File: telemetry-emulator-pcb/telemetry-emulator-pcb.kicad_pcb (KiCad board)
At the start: 2 copper layers, 100 x 50 mm, 53 parts, among them IC1 ATmega328P-A, IC2 MCP2515-xSO, IC3 MCP2551-I-SN, J1 USB_B_Micro, J2 ENABLE_RX, J3 Conn_02x13_Odd_Even, J4 CAN_TERM, J5 USE_V_INT, J6 UART, J7 CAN, J8 CAN, J9 CAN, Q1 BSS138, Q2 BSS138, U1 CH340C, Y1 16MHz, Y2 8MHz

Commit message: done and done
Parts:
- added R7: 10K, Resistor_SMD:R_0805_2012Metric, F.Cu at (100.5, 78.5)
- renumbered R9 to R10, R10 to R11, R11 to R12, R12 to R13, R7 to R8, R8 to R9
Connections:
- IC2 pad 17: +5V -> Net-(IC2-Pad17)
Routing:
- net Net-(IC2-Pad17): track 0.00 -> 14.0 mm, vias 0 -> 2
- net MOSI: track 70.1 -> 72.8 mm
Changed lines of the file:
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@@
   (net 66 "Net-(J4-Pad1)")
   (net 67 "V_EXT")
+  (net 68 "Net-(IC2-Pad17)")
   (footprint "Capacitor_SMD:C_0805_2012Metric" (layer "F.Cu")
     (at 157.48 92.642)
@@
     (property "Sheetname" "")
     (attr smd)
-    (fp_text reference "R11" (at 2.653 0.0325 180) (layer "F.SilkS")
+    (fp_text reference "R12" (at 2.653 0.0325 180) (layer "F.SilkS")
       (effects (font (size 1 1) (thickness 0.15)))
     )
@@
       (net 21 "CAN_CS") (pinfunction "~{CS}") (pintype "input"))
     (pad "17" smd roundrect (at 4.65 -3.81 270) (size 2.05 0.6) (layers "F.Cu" "F.Paste" "F.Mask") (roundrect_rratio 0.25)
-      (net 1 "+5V") (pinfunction "~{RESET}") (pintype "input"))
+      (net 68 "Net-(IC2-Pad17)") (pinfunction "~{RESET}") (pintype "input"))
     (pad "18" smd roundrect (at 4.65 -5.08 270) (size 2.05 0.6) (layers "F.Cu" "F.Paste" "F.Mask") (roundrect_rratio 0.25)
       (net 1 "+5V") (pinfunction "VDD") (pintype "power_in"))
@@
     (property "Sheetname" "")
     (attr smd)
-    (fp_text reference "R9" (at 0 -1.65 90) (layer "F.SilkS")
+    (fp_text reference "R10" (at 0 -1.65 90) (layer "F.SilkS")
       (effects (font (size 1 1) (thickness 0.15)))
     )
@@
     (property "Sheetname" "")
     (attr smd)
-    (fp_text reference "R12" (at 0 -1.65) (layer "F.SilkS")
+    (fp_text reference "R13" (at 0 -1.65) (layer "F.SilkS")
       (effects (font (size 1 1) (thickness 0.15)))
     )
@@
   )
   (footprint "Resistor_SMD:R_0805_2012Metric" (layer "F.Cu")
+    (at 100.5 78.5 90)
+    (descr "Resistor SMD 0805 (2012 Metric), square (rectangular) end terminal, IPC_7351 nominal, (Body size source: IPC-SM-782 page 72, https://www.pcb-3d.com/wordpress/wp-content/uploads/ipc-sm-782a_amendment_1_and_2.pdf), generated with kicad-footprint-generator")
+    (tags "resistor")
+    (property "Sheetfile" "telemetry-emulator-pcb.kicad_sch")
+    (property "Sheetname" "")
+    (attr smd)
+    (fp_text reference "R7" (at 2.4 0 180) (layer "F.SilkS")
+      (effects (font (size 1 1) (thickness 0.15)))
+    )
+    (fp_text value "10K" (at 0.2 -1.7 270) (layer "F.Fab")
+      (effects (font (size 1 1) (thickness 0.15)))
+    )
+    (fp_text user "${REFERENCE}" (at 0 0 90) (layer "F.Fab")
+      (effects (font (size 0.5 0.5) (thickness 0.08)))
+    )
+    (fp_line (start -0.227064 0.735) (end 0.227064 0.735) (layer "F.SilkS") (width 0.12))
+    (fp_line (start -0.227064 -0.735) (end 0.227064 -0.735) (layer "F.SilkS") (width 0.12))
+    (fp_line (start 1.68 -0.95) (end 1.68 0.95) (layer "F.CrtYd") (width 0.05))
+    (fp_line (start -1.68 0.95) (end -1.68 -0.95) (layer "F.CrtYd") (width 0.05))
+    (fp_line (start -1.68 -0.95) (end 1.68 -0.95) (layer "F.CrtYd") (width 0.05))
+    (fp_line (start 1.68 0.95) (end -1.68 0.95) (layer "F.CrtYd") (width 0.05))
+    (fp_line (start 1 0.625) (end -1 0.625) (layer "F.Fab") (width 0.1))
+    (fp_line (start -1 -0.625) (end 1 -0.625) (layer "F.Fab") (width 0.1))
+    (fp_line (start 1 -0.625) (end 1 0.625) (layer "F.Fab") (width 0.1))
+    (fp_line (start -1 0.625) (end -1 -0.625) (layer "F.Fab") (width 0.1))
+    (pad "1" smd roundrect (at -0.9125 0 90) (size 1.025 1.4) (layers "F.Cu" "F.Paste" "F.Mask") (roundrect_rratio 0.243902)
+      (net 68 "Net-(IC2-Pad17)") (pintype "passive"))
+    (pad "2" smd roundrect (at 0.9125 0 90) (size 1.025 1.4) (layers "F.Cu" "F.Paste" "F.Mask") (roundrect_rratio 0.243902)
+      (net 1 "+5V") (pintype "passive"))
+    (model "${KICAD6_3DMODEL_DIR}/Resistor_SMD.3dshapes/R_0805_2012Metric.wrl"
+      (offset (xyz 0 0 0))
+      (scale (xyz 1 1 1))
+      (rotate (xyz 0 0 0))
+    )
+  )
+  (footprint "Resistor_SMD:R_0805_2012Metric" (layer "F.Cu")
     (at 158.7325 79.8595 -90)
     (descr "Resistor SMD 0805 (2012 Metric), square (rectangular) end terminal, IPC_7351 nominal, (Body size source: IPC-SM-782 page 72, https://www.pcb-3d.com/wordpress/wp-content/uploads/ipc-sm-782a_amendment_1_and_2.pdf), generated with kicad-footprint-generator")
@@
     (property "Sheetname" "")
     (attr smd)
-    (fp_text reference "R7" (at -2.4595 0.0325 180) (layer "F.SilkS")
+    (fp_text reference "R8" (at -2.4595 0.0325 180) (layer "F.SilkS")
       (effects (font (size 1 1) (thickness 0.15)))
     )
@@
     (property "Sheetname" "")
     (attr smd)
-    (fp_text reference "R10" (at -2.4595 0.0325 180) (layer "F.SilkS")
+    (fp_text reference "R11" (at -2.4595 0.0325 180) (layer "F.SilkS")
       (effects (font (size 1 1) (thickness 0.15)))
     )
@@
     (property "Sheetname" "")
     (attr smd)
-    (fp_text reference "R8" (at 2.6405 0.0325 180) (layer "F.SilkS")
+    (fp_text reference "R9" (at 2.6405 0.0325 180) (layer "F.SilkS")
       (effects (font (size 1 1) (thickness 0.15)))
     )
@@
   (segment (start 136.684 89.73) (end 136.684 84.106) (width 0.25) (layer "F.Cu") (net 9))
   (segment (start 136 91.3) (end 136 91.274198) (width 0.25) (layer "F.Cu") (net 9))
+  (segment (start 108.6 77.9) (end 108.712 78.012) (width 0.25) (layer "F.Cu") (net 9))
   (segment (start 136.687099 89.733099) (end 136.684 89.73) (width 0.25) (layer "F.Cu") (net 9))
   (segment (start 136 91.274198) (end 136.687099 90.587099) (width 0.25) (layer "F.Cu") (net 9))
+  (segment (start 108.712 78.012) (end 108.712 83.136) (width 0.25) (layer "F.Cu") (net 9))
   (segment (start 136.687099 90.587099) (end 136.687099 89.733099) (width 0.25) (layer "F.Cu") (net 9))
-  (segment (start 108.712 79.912) (end 108.712 83.136) (width 0.25) (layer "F.Cu") (net 9))
   (segment (start 136.684 84.106) (end 133.35 80.772) (width 0.25) (layer "F.Cu") (net 9))
-  (segment (start 108.7 79.9) (end 108.712 79.912) (width 0.25) (layer "F.Cu") (net 9))
-  (via (at 108.7 79.9) (size 0.8) (drill 0.4) (layers "F.Cu" "B.Cu") (free) (net 9))
+  (via (at 108.6 77.9) (size 0.8) (drill 0.4) (layers "F.Cu" "B.Cu") (free) (net 9))
   (via (at 136 91.3) (size 0.8) (drill 0.4) (layers "F.Cu" "B.Cu") (free) (net 9))
-  (segment (start 130.1 79.5) (end 132.078 79.5) (width 0.25) (layer "B.Cu") (net 9))
+  (segment (start 131.985 79.407) (end 133.35 80.772) (width 0.25) (layer "B.Cu") (net 9))
   (segment (start 115.54 103.46) (end 114.94 103.46) (width 0.25) (layer "B.Cu") (net 9))
-  (segment (start 132.078 79.5) (end 133.35 80.772) (width 0.25) (layer "B.Cu") (net 9))
+  (segment (start 128.828 78.6) (end 129.635 79.407) (width 0.25) (layer "B.Cu") (net 9))
   (segment (start 135.5 90.8) (end 135.5 89.5) (width 0.25) (layer "B.Cu") (net 9))
-  (segment (start 108.7 79.9) (end 129.7 79.9) (width 0.25) (layer "B.Cu") (net 9))
-  (segment (start 129.7 79.9) (end 130.1 79.5) (width 0.25) (layer "B.Cu") (net 9))
   (segment (start 135.5 89.5) (end 135 89) (width 0.25) (layer "B.Cu") (net 9))
+  (segment (start 129.635 79.407) (end 131.985 79.407) (width 0.25) (layer "B.Cu") (net 9))
   (segment (start 135 89) (end 130.036396 89) (width 0.25) (layer "B.Cu") (net 9))
+  (segment (start 108.6 77.9) (end 109.3 78.6) (width 0.25) (layer "B.Cu") (net 9))
   (segment (start 130.036396 89) (end 115.576396 103.46) (width 0.25) (layer "B.Cu") (net 9))
   (segment (start 115.576396 103.46) (end 114.94 103.46) (width 0.25) (layer "B.Cu") (net 9))
   (segment (start 136 91.3) (end 135.5 90.8) (width 0.25) (layer "B.Cu") (net 9))
+  (segment (start 109.3 78.6) (end 128.828 78.6) (width 0.25) (layer "B.Cu") (net 9))
   (segment (start 137.4 95.621) (end 139.084 97.305) (width 0.25) (layer "F.Cu") (net 10))
   (segment (start 137.4 95.1045) (end 137.4 95.621) (width 0.25) (layer "F.Cu") (net 10))
@@
   (segment (start 173.078897 80.039897) (end 171.2885 78.2495) (width 0.25) (layer "B.Cu") (net 67))
   (segment (start 171.9305 87.4) (end 173.078897 86.251603) (width 0.25) (layer "B.Cu") (net 67))
+  (via (at 112.5 83.2) (size 0.8) (drill 0.4) (layers "F.Cu" "B.Cu") (net 68))
+  (via (at 100.5 79.4) (size 0.8) (drill 0.4) (layers "F.Cu" "B.Cu") (net 68))
+  (segment (start 102.3 81.2) (end 111.3 81.2) (width 0.25) (layer "B.Cu") (net 68))
+  (segment (start 100.5 79.4) (end 102.3 81.2) (width 0.25) (layer "B.Cu") (net 68))
+  (segment (start 111.3 81.2) (end 112.5 82.4) (width 0.25) (layer "B.Cu") (net 68))
+  (segment (start 112.5 82.4) (end 112.5 83.2) (width 0.25) (layer "B.Cu") (net 68))
   (zone (net 1) (net_name "+5V") (layer "F.Cu") (name "5V") (hatch edge 0.508)
     (connect_pads (clearance 0.508))

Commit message: Board is finished
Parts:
- removed the C3 at (108.2, 88.7)
- removed the C3 at (94.3, 73.7)
- added C3: 10uF, Capacitor_SMD:C_1206_3216Metric, F.Cu at (94.4, 73.2)
- added C7: 0.1uF, Capacitor_SMD:C_0805_2012Metric, F.Cu at (108.2, 88.7)
- added D5: Schottky, Diode_SMD:D_SOD-323, F.Cu at (170.4, 71.4)
- C1: footprint Capacitor_SMD:C_0805_2012Metric -> Diode_SMD:D_SOD-323
- D2: value purple -> red
- IC1: value ATmega328P-A -> ATmega328P
- IC2: value MCP2515-xSO -> MCP2515
- IC3: value MCP2551-I-SN -> MCP2551
- J1: value USB_B_Micro -> USB
- J2: value ENABLE_RX -> RX_TX; footprint Connector_PinHeader_2.54mm:PinHeader_1x02_P2.54mm_Vertical -> Connector_PinHeader_2.54mm:PinHeader_2x02_P2.54mm_Vertical
- J3: value Conn_02x13_Odd_Even -> GPIO
- J5: value USE_V_INT -> V_INT
- R1: value 1K -> 1.2K
- R2: value 500 -> 1.5K
- R3: value 1K -> 1.5K
- R4: value 500 -> 1.2K
- moved J5 3.50 mm to (174.9, 93.9)
- moved J2 3.30 mm to (168.4, 96.6), turned to 90 degrees
- turned C2 to -90 degrees
- renumbered C8 to C10, C9 to C11, C10 to C12, C11 to C13, C2 to C4, C4 to C5, C5 to C6, C6 to C8, C7 to C9
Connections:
- C2 pad 1: +5V -> Earth
- C2 pad 2: Earth -> +5V
- IC1 pad 31: TX -> TX_USB
- J2 pad 1: RX -> RX_USB
- J2 pad 2: RX_USB -> RX
- J3 pad 26: TX -> TX_USB
- J6 pad 1: V_EXT -> Net-(D5-Pad2)
- J7 pad 1: CANH -> CANL
- J7 pad 2: CANL -> CANH
- J8 pad 1: CANH -> CANL
- J8 pad 2: CANL -> CANH
- J9 pad 1: CANH -> CANL
- J9 pad 2: CANL -> CANH
- R13 pad 2: CANL -> CANH
- R6 pad 1: TX -> TX_USB
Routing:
- net TX_USB: track 0.00 -> 60.4 mm, vias 0 -> 2
- net TX: track 78.4 -> 22.1 mm, vias 5 -> 1
- net CANL: track 58.2 -> 40.5 mm
- net Net-(D5-Pad2): track 0.00 -> 8.37 mm
- net CANH: track 51.2 -> 57.2 mm
- net V_EXT: track 44.1 -> 47.8 mm, vias 2 -> 3
- net RX_USB: track 58.3 -> 61.2 mm, vias 2 -> 3
- net D7: track 55.5 -> 53.8 mm
- net D6: track 51.4 -> 49.9 mm
- net +5V: track 24.0 -> 24.8 mm
- net D5: track 43.2 -> 42.4 mm
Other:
- board text added: "Colby Sparks Silviu Toderita"
- board text added: "Telemetry Emulator 1.0"
- board text added: "UBC Supermileage"

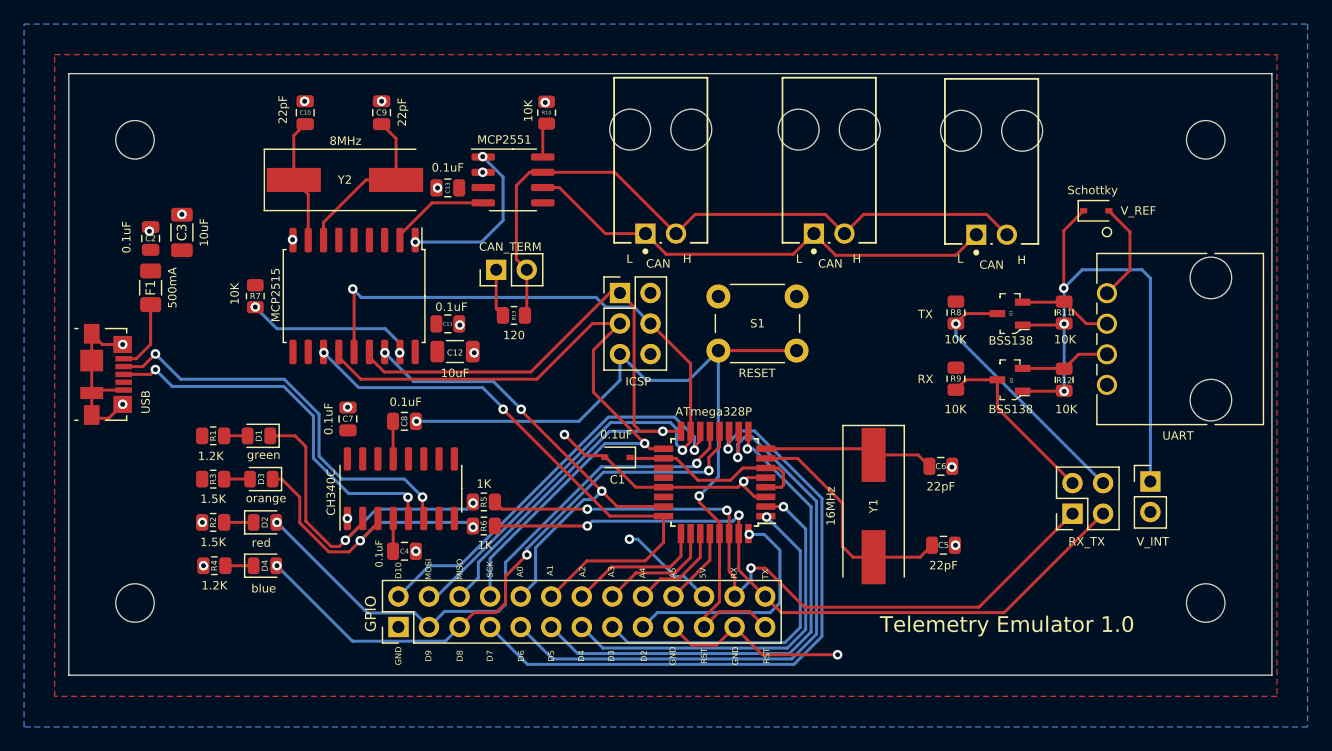
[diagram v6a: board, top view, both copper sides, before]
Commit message: adds rounded edges to pcb and modifies xtal resistance
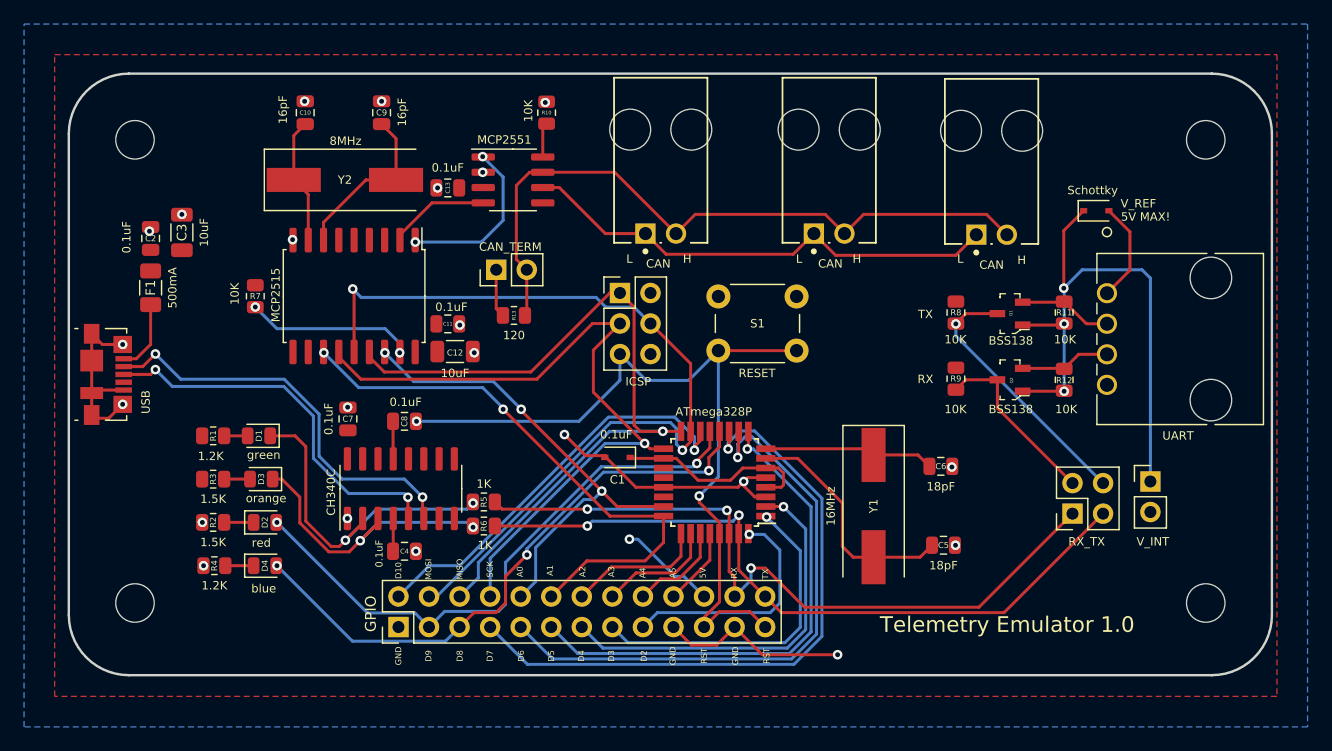
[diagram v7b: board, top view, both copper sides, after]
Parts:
- C10, C9: value 22pF -> 16pF
- C5, C6: value 22pF -> 18pF
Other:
- outline, holes or cut-outs redrawn
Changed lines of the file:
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@@
       (effects (font (size 0.7 0.7) (thickness 0.1)))
     )
-    (fp_text value "22pF" (at 0 1.68) (layer "F.SilkS")
+    (fp_text value "18pF" (at 0 1.68) (layer "F.SilkS")
       (effects (font (size 0.7 0.7) (thickness 0.1)))
     )
@@
       (effects (font (size 0.7 0.7) (thickness 0.1)))
     )
-    (fp_text value "22pF" (at 0 1.68) (layer "F.SilkS")
+    (fp_text value "18pF" (at 0 1.68) (layer "F.SilkS")
       (effects (font (size 0.7 0.7) (thickness 0.1)))
     )
@@
       (effects (font (size 0.7 0.7) (thickness 0.1)))
     )
-    (fp_text value "22pF" (at 0.246 -1.848 90) (layer "F.SilkS")
+    (fp_text value "16pF" (at 0.246 -1.848 90) (layer "F.SilkS")
       (effects (font (size 0.7 0.7) (thickness 0.1)))
     )
@@
       (effects (font (size 0.7 0.7) (thickness 0.1)))
     )
-    (fp_text value "22pF" (at 0.046 1.702 90) (layer "F.SilkS")
+    (fp_text value "16pF" (at 0.046 1.702 90) (layer "F.SilkS")
       (effects (font (size 0.7 0.7) (thickness 0.1)))
     )
@@
       (effects (font (size 0.7 0.7) (thickness 0.1)))
     )
-    (fp_text user "V_REF" (at -6.8495 -2.6115) (layer "F.SilkS")
+    (fp_text user "V_REF" (at -7.4495 -2.6115) (layer "F.SilkS")
+      (effects (font (size 0.7 0.7) (thickness 0.08)))
+    )
+    (fp_text user "5V MAX!" (at -6.3495 -3.2115) (layer "F.SilkS")
       (effects (font (size 0.7 0.7) (thickness 0.08)))
     )
@@
     )
   )
+  (gr_arc (start 180 60) (mid 183.535534 61.464466) (end 185 65) (layer "Edge.Cuts") (width 0.2))
+  (gr_line (start 90 110) (end 180 110) (layer "Edge.Cuts") (width 0.2))
   (gr_rect (start 185 110) (end 185 110) (layer "Edge.Cuts") (width 0.1) (fill none))
-  (gr_rect (start 85 60) (end 185 110) (layer "Edge.Cuts") (width 0.1) (fill none))
+  (gr_line (start 185 105) (end 185 65) (layer "Edge.Cuts") (width 0.2))
+  (gr_arc (start 185 105) (mid 183.535534 108.535534) (end 180 110) (layer "Edge.Cuts") (width 0.2))
+  (gr_line (start 85 105) (end 85 65) (layer "Edge.Cuts") (width 0.2))
+  (gr_arc (start 85 65) (mid 86.464466 61.464466) (end 90 60) (layer "Edge.Cuts") (width 0.2))
+  (gr_arc (start 90 110) (mid 86.464466 108.535534) (end 85 105) (layer "Edge.Cuts") (width 0.2))
+  (gr_line (start 90 60) (end 180 60) (layer "Edge.Cuts") (width 0.2))
   (gr_text "UBC Supermileage" (at 104.8 70 180) (layer "B.SilkS")
     (effects (font (size 1.3 1.3) (thickness 0.25) italic) (justify mirror))

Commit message: adds supermileage logo
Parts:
- added G***: LOGO, telemetry-emulator-pcb:sm_logo, B.Cu at (111.8, 91.4)
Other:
- board text removed: "UBC Supermileage"
